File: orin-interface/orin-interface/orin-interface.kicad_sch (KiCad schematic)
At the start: 0 parts

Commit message: Finished: Orin-BoB
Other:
- added sheet Step_Down_Conv (Step_Down_Conv.kicad_sch)
- sheet CAN_CONN ports: added PWM; removed +3V3, GPIO_IN
- sheet Power_CON ports: added +BATT_P; removed +BATT
- sheet Standard_CONN ports: added PWM; removed none
- note removed: "Husk 3v3 Regulator"

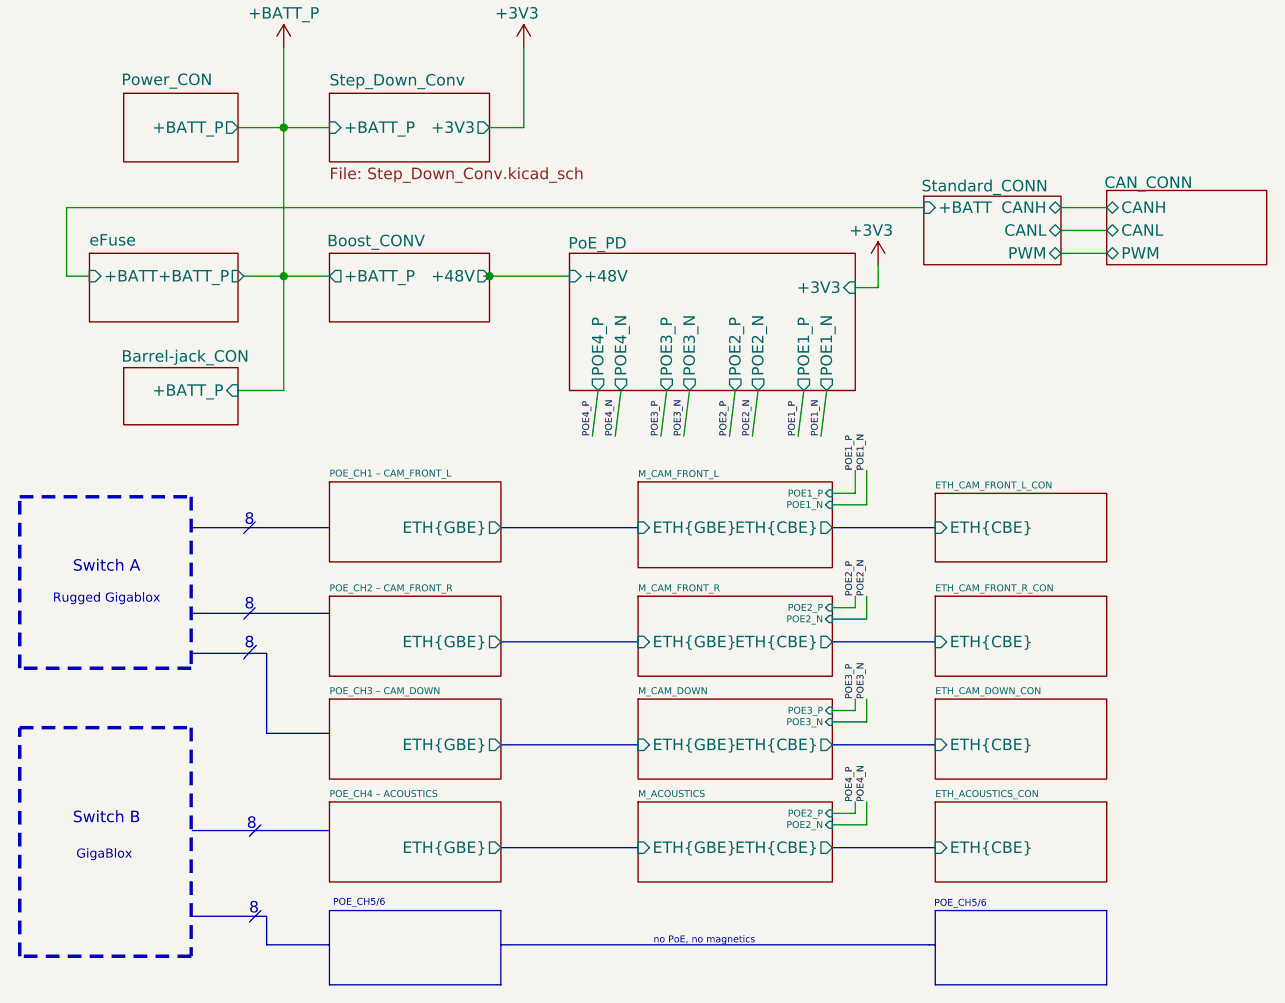
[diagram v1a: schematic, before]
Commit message: orin-interface: PoE channels, buses, 3V3 regulator, ERC fixes
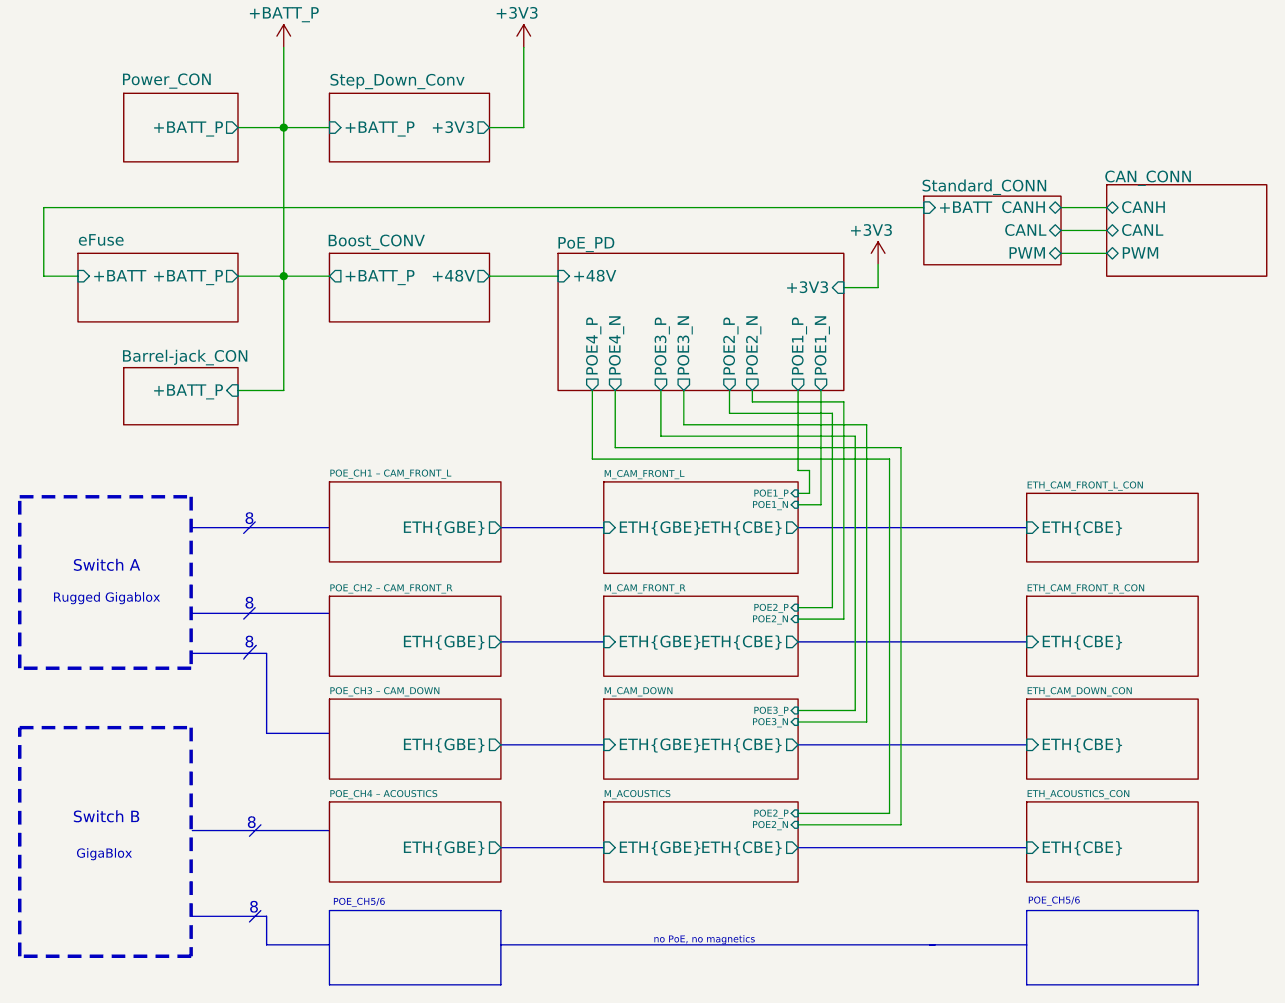
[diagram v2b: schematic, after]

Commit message: orin-interface: add ETH connector sheets and Mate-connectors footprint lib; update orin-bob
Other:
- sheet ETH_ACOUSTICS_CON: file ETH_CAM1_CON.kicad_sch -> ETH_ACOUSTICS_CON.kicad_sch
- sheet ETH_CAM_DOWN_CON: file ETH_CAM1_CON.kicad_sch -> ETH_CAM_DOWN_CON.kicad_sch
- sheet ETH_CAM_FRONT_L_CON: file ETH_CAM1_CON.kicad_sch -> ETH_CAM_FRONT_O.kicad_sch
- sheet ETH_CAM_FRONT_R_CON: file ETH_CAM1_CON.kicad_sch -> ETH_CAM_FRONT_R.kicad_sch

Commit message: finished v2 schematic
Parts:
- added C25, C62: 4.7uF, Capacitor_SMD:C_0603_1608Metric_Pad1.08x0.95mm_HandSolder, symbol Device:C_Small
- added C63: 22uF, Capacitor_SMD:C_0603_1608Metric_Pad1.08x0.95mm_HandSolder, symbol Device:C_Small
- added J10: 694106402002, 694106402002:J_Wurth_WR-DC_694106402002, symbol 694106402002:694106402002
- added J12, J13, J15, J9: 615008142521, 615008138021-THT:J_Wurth_WR-MJ_615008142521, symbol WR-MJ:615008142521
- added J14, J18, J19, J20: 634008138121, 615008138021:J_Wurth_WR-MJ_634008138121, symbol WR-MJ:634008138121
- added J17, J21: 64600411622, Wurth_WR-WTB:J_Wurth_WR-WTB_64600411622, symbol WR-WTB:64600411622
- added L3: 1pH, Inductor_SMD:L_0201_0603Metric_Pad0.64x0.40mm_HandSolder, symbol Device:L_Small
- added U4: 173950336, MagIC_THT_Wurth:U_Wurth_WPME-FDSM_17395xx36, symbol 173950336:173950336
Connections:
- net +3V3: now also C63.1, U4.3 (VOUT)
- net +BATT_P: now also C25.1, J10.1, J17.3, J17.4, J21.3, J21.4, L3.1
- new net: C62.1, L3.2, U4.1 (VIN)
- new net ETH.D1+: J14.1, J18.1, J19.1, J20.1
- new net ETH.D1-: J14.2, J18.2, J19.2, J20.2
- new net ETH.D2+: J14.3, J18.3, J19.3, J20.3
- new net ETH.D2-: J14.4, J18.4, J19.4, J20.4
- new net ETH.D3+: J14.5, J18.5, J19.5, J20.5
- new net ETH.D3-: J14.6, J18.6, J19.6, J20.6
- new net ETH.D4+: J14.7, J18.7, J19.7, J20.7
- new net ETH.D4-: J14.8, J18.8, J19.8, J20.8
- new net ETH.X1+: J12.1, J13.1, J15.8, J9.8
- new net ETH.X1-: J12.2, J13.2, J15.7, J9.7
- new net ETH.X2+: J12.3, J13.3, J15.6, J9.6
- new net ETH.X2-: J12.4, J13.4, J15.5, J9.5
- new net ETH.X3+: J12.5, J13.5, J15.4, J9.4
- new net ETH.X3-: J12.6, J13.6, J15.3, J9.3
- new net ETH.X4+: J12.7, J13.7, J15.2, J9.2
- new net ETH.X4-: J12.8, J13.8, J15.1, J9.1
- new net GND: C25.2, C62.2, C63.2, J10.2, J10.3, J17.1, J17.2, J21.1, J21.2, U4.2 (GND)
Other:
- removed sheet Barrel-jack_CON
- removed sheet CAN_CONN
- removed sheet ETH_ACOUSTICS_CON
- removed sheet ETH_CAM_DOWN_CON
- removed sheet ETH_CAM_FRONT_L_CON
- removed sheet ETH_CAM_FRONT_R_CON
- removed sheet POE_CH1 – CAM_FRONT_L
- removed sheet POE_CH2 – CAM_FRONT_R
- removed sheet POE_CH3 – CAM_DOWN
- removed sheet POE_CH4 – ACOUSTICS
- removed sheet Power_CON
- removed sheet Standard_CONN
- removed sheet Step_Down_Conv
- sheet M_ACOUSTICS ports: added POE4_N, POE4_P; removed POE2_N, POE2_P
- note added: "Barrel-Jack"
- note added: "Ethernet - ACOUSTICS"
- note added: "Ethernet - Camera (Down)"
- note added: "Ethernet - Camera (Left)"
- note added: "Ethernet - Camera (Right)"
- note added: "Non-poe device"
- note added: "Power Outputs"
- note added: "Power for GigaBlox"
- note added: "Power for Rugged GigaBlox"
- note added: "VBAT_P -> 3V3 Converter"
- note removed: "POE_CH5/6"
- note removed: "no PoE, no magnetics"

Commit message: Still developing
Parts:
- removed J12, J13, J15, J9: 615008142521, 615008138021-THT:J_Wurth_WR-MJ_615008142521, symbol WR-MJ:615008142521
- removed J14, J18, J19, J20: 634008138121, 615008138021:J_Wurth_WR-MJ_634008138121, symbol WR-MJ:634008138121
- added J1: 691323100002, 691378140024-2:J_Wurth_WR-TBL_691323100002, symbol 691323100002:691323100002
- added J11: 615008160421, 615008138021-THT:J_Wurth_WR-MJ_615008160421, symbol 615008160421:615008160421
- added J2, J8, J9: 615008160421, 615008160421:J_Wurth_WR-MJ_615008160421, symbol 615008160421:615008160421
- added J3, J4, J5, J6: 615008160721, 615008160721:J_Wurth_WR-MJ_615008160721, symbol 615008160721:615008160721
- L3: footprint Inductor_SMD:L_0201_0603Metric_Pad0.64x0.40mm_HandSolder -> Inductor_SMD:L_0603_1608Metric
- U4: footprint MagIC_THT_Wurth:U_Wurth_WPME-FDSM_17395xx36 -> 173950336:U_Wurth_WPME-FDSM_17395xx36
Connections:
- net ETH.D1+: now also J11.1, J2.1, J8.8, J9.1
- net ETH.D1-: now also J11.2, J2.2, J8.7, J9.2
- net ETH.D2+: now also J11.3, J2.3, J8.6, J9.3
- net ETH.D2-: now also J11.4, J2.4, J8.5, J9.4
- net ETH.D3+: now also J11.5, J2.5, J8.4, J9.6
- net ETH.D3-: now also J11.6, J2.6, J8.3, J9.5
- net ETH.D4+: now also J11.7, J2.7, J8.2, J9.7
- net ETH.D4-: now also J11.8, J2.8, J8.1, J9.8
- net ETH.X1+: now also J3.8, J4.8, J5.1, J6.8
- net ETH.X1-: now also J3.7, J4.7, J5.2, J6.7
- net ETH.X2+: now also J3.6, J4.6, J5.3, J6.6
- net ETH.X2-: now also J3.5, J4.5, J5.4, J6.5
- net ETH.X3+: now also J3.4, J4.4, J5.5, J6.4
- net ETH.X3-: now also J3.3, J4.3, J5.6, J6.3
- net ETH.X4+: now also J3.2, J4.2, J5.7, J6.2
- net ETH.X4-: now also J3.1, J4.1, J5.8, J6.1
- net GND: now also J1.1, J11.Z1 (SHIELD), J11.Z2 (SHIELD), J2.Z1 (SHIELD), J2.Z2 (SHIELD), J3.S1 (SHIELD), J3.S2 (SHIELD), J4.S1 (SHIELD), J4.S2 (SHIELD), J5.S1 (SHIELD), J5.S2 (SHIELD), J6.S1 (SHIELD), J6.S2 (SHIELD), J8.Z1 (SHIELD), J8.Z2 (SHIELD), J9.Z1 (SHIELD), J9.Z2 (SHIELD)
- new net +BATT: J1.2
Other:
- note added: "Power Input"
